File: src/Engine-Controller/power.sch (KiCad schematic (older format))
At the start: 0 parts

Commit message: Completed power supply part of schematic
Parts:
- added C? (x2): 10uF, CWR11C_KEM, symbol Engine-Controller:CWR11HH106KB
- added C?: 22uF, symbol Engine-Controller:UKL1C220KDDANATD
- added C?: 2.2uF, symbol Engine-Controller:CAP_0603
- added C?: 1 uF, symbol Engine-Controller:CAP_0603
- added C?: 10 nF, symbol Engine-Controller:CAP_0603
- added C?: 120uF, symbol Engine-Controller:UHE2A121MHD6
- added D?: LTST-C150GKT, symbol Engine-Controller:LTST-C150GKT
- added D?: Schottky, symbol Engine-Controller:Schottky
- added J?: 4840.2201, CONN_4840.2201_SCH, symbol Engine-Controller:4840.2201
- added L?: 22uH, symbol Engine-Controller:CBC3225T220KR
- added R?: 976, symbol Engine-Controller:RES_0603
- added R?: 240, symbol Engine-Controller:RES_0603
- added R?: 470k, symbol Engine-Controller:RES_0805
- added R?: 1.54k, symbol Engine-Controller:RES_0805
- added U?: LMS8117AMP-3.3_NOPB, symbol Engine-Controller:LMS8117AMP-3.3_NOPB
- added U?: LM22672MRE-5.0_NOPB, symbol Engine-Controller:LM22672MRE-5.0_NOPB
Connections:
- net labels added: 3.3V, 5V, Earth, VIN
- wire segments 0 -> 55

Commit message: Annotated Schematic
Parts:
- gave numbers to parts that had none: 17
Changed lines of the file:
@@
 $EndDescr
 $Comp
-L Engine-Controller:LTST-C150GKT D?
+L Engine-Controller:LTST-C150GKT D3
 U 1 1 60EB9E6E
 P 9300 4350
-F 0 "D?" H 9529 4453 60  0000 L CNN
+F 0 "D3" H 9529 4453 60  0000 L CNN
 F 1 "LTST-C150GKT" H 9529 4347 60  0001 L CNN
 F 2 "" H 9500 3990 60  0001 C CNN
@@
 $EndComp
 $Comp
-L Engine-Controller:CBC3225T220KR L?
+L Engine-Controller:CBC3225T220KR L1
 U 1 1 60EBAB6D
 P 6150 4000
-F 0 "L?" H 6150 4181 50  0000 C CNN
+F 0 "L1" H 6150 4181 50  0000 C CNN
 F 1 "22uH" H 6150 4100 50  0000 C CNN
 F 2 "" H 6000 3800 50  0001 L BNN
@@
 $EndComp
 $Comp
-L Engine-Controller:Schottky D?
+L Engine-Controller:Schottky D2
 U 1 1 60EBB138
 P 5650 4250
-F 0 "D?" V 5650 4330 50  0000 L CNN
+F 0 "D2" V 5650 4330 50  0000 L CNN
 F 1 "Schottky" V 5695 4330 50  0001 L CNN
 F 2 "" H 5650 4250 50  0001 C CNN
@@
 $EndComp
 $Comp
-L Engine-Controller:LMS8117AMP-3.3_NOPB U?
+L Engine-Controller:LMS8117AMP-3.3_NOPB U3
 U 1 1 60EBB9CF
 P 8100 4050
-F 0 "U?" H 8100 4365 50  0000 C CNN
+F 0 "U3" H 8100 4365 50  0000 C CNN
 F 1 "LMS8117AMP-3.3_NOPB" H 8100 4274 50  0000 C CNN
 F 2 "" H 8100 4050 50  0001 C CNN
@@
 $EndComp
 $Comp
-L Engine-Controller:4840.2201 J?
+L Engine-Controller:4840.2201 J1
 U 1 1 60EBBEC5
 P 2450 3500
-F 0 "J?" H 2692 3787 60  0000 C CNN
+F 0 "J1" H 2692 3787 60  0000 C CNN
 F 1 "4840.2201" H 2692 3681 60  0000 C CNN
 F 2 "CONN_4840.2201_SCH" H 2850 2900 60  0001 C CNN
@@
 $EndComp
 $Comp
-L power:Earth #PWR?
+L power:Earth #PWR0103
 U 1 1 60EC7BCD
 P 2600 3950
-F 0 "#PWR?" H 2600 3700 50  0001 C CNN
+F 0 "#PWR0103" H 2600 3700 50  0001 C CNN
 F 1 "Earth" H 2600 3800 50  0001 C CNN
 F 2 "" H 2600 3950 50  0001 C CNN
@@
 	2850 3500 2450 3500
 $Comp
-L Engine-Controller:UKL1C220KDDANATD C?
+L Engine-Controller:UKL1C220KDDANATD C1
 U 1 1 60EDB6C2
 P 2850 3900
-F 0 "C?" H 2965 3946 50  0000 L CNN
+F 0 "C1" H 2965 3946 50  0000 L CNN
 F 1 "22uF" H 2965 3855 50  0000 L CNN
 F 2 "" H 2850 3900 50  0001 C CNN
@@
 	2850 3750 2850 3500
 $Comp
-L power:Earth #PWR?
+L power:Earth #PWR0104
 U 1 1 60EE05FF
 P 2850 4200
-F 0 "#PWR?" H 2850 3950 50  0001 C CNN
+F 0 "#PWR0104" H 2850 3950 50  0001 C CNN
 F 1 "Earth" H 2850 4050 50  0001 C CNN
 F 2 "" H 2850 4200 50  0001 C CNN
@@
 	2850 4050 2850 4200
 $Comp
-L Engine-Controller:CAP_0603 C?
+L Engine-Controller:CAP_0603 C2
 U 1 1 60EE1F59
 P 3300 3900
-F 0 "C?" V 3254 4003 50  0000 L CNN
+F 0 "C2" V 3254 4003 50  0000 L CNN
 F 1 "2.2uF" V 3345 4003 50  0000 L CNN
 F 2 "" H 3200 3500 50  0001 L BNN
@@
 $EndComp
 $Comp
-L power:Earth #PWR?
+L power:Earth #PWR0105
 U 1 1 60EE39C4
 P 3300 4200
-F 0 "#PWR?" H 3300 3950 50  0001 C CNN
+F 0 "#PWR0105" H 3300 3950 50  0001 C CNN
 F 1 "Earth" H 3300 4050 50  0001 C CNN
 F 2 "" H 3300 4200 50  0001 C CNN
@@
 	3300 3750 3300 3500
 $Comp
-L Engine-Controller:RES_0805 R?
+L Engine-Controller:RES_0805 R2
 U 1 1 60EEF47A
 P 3900 3600
-F 0 "R?" H 4050 3700 50  0000 C CNN
+F 0 "R2" H 4050 3700 50  0000 C CNN
 F 1 "470k" H 3800 3700 50  0000 C CNN
 F 2 "" H 3950 3100 50  0001 L BNN
@@
 $EndComp
 $Comp
-L Engine-Controller:CAP_0603 C?
+L Engine-Controller:CAP_0603 C3
 U 1 1 60EF8CF7
 P 4900 4050
-F 0 "C?" V 4854 4153 50  0000 L CNN
+F 0 "C3" V 4854 4153 50  0000 L CNN
 F 1 "1 uF" V 4945 4153 50  0000 L CNN
 F 2 "" H 4800 3650 50  0001 L BNN
@@
 	4900 3800 4900 3900
 $Comp
-L power:Earth #PWR?
+L power:Earth #PWR0106
 U 1 1 60F2A939
 P 4900 4650
-F 0 "#PWR?" H 4900 4400 50  0001 C CNN
+F 0 "#PWR0106" H 4900 4400 50  0001 C CNN
 F 1 "Earth" H 4900 4500 50  0001 C CNN
 F 2 "" H 4900 4650 50  0001 C CNN
@@
 	4900 3700 5400 3700
 $Comp
-L Engine-Controller:CAP_0603 C?
+L Engine-Controller:CAP_0603 C4
 U 1 1 60F34E40
 P 5650 3750
-F 0 "C?" V 5604 3853 50  0000 L CNN
+F 0 "C4" V 5604 3853 50  0000 L CNN
 F 1 "10 nF" V 5695 3853 50  0000 L CNN
 F 2 "" H 5550 3350 50  0001 L BNN
@@
 	4300 3800 4300 3950
 $Comp
-L power:Earth #PWR?
+L power:Earth #PWR0107
 U 1 1 60F261A1
 P 4300 3950
-F 0 "#PWR?" H 4300 3700 50  0001 C CNN
+F 0 "#PWR0107" H 4300 3700 50  0001 C CNN
 F 1 "Earth" H 4300 3800 50  0001 C CNN
 F 2 "" H 4300 3950 50  0001 C CNN
@@
 $EndComp
 $Comp
-L Engine-Controller:LM22672MRE-5.0_NOPB U?
+L Engine-Controller:LM22672MRE-5.0_NOPB U2
 U 1 1 60F0F687
 P 4600 3700
-F 0 "U?" H 4600 4115 50  0000 C CNN
+F 0 "U2" H 4600 4115 50  0000 C CNN
 F 1 "LM22672MRE-5.0_NOPB" H 4600 4024 50  0000 C CNN
 F 2 "" H 4550 3700 50  0001 C CNN
@@
 Connection ~ 5650 4000
 $Comp
-L Engine-Controller:UHE2A121MHD6 C?
+L Engine-Controller:UHE2A121MHD6 C5
 U 1 1 60F87FD5
 P 6650 4250
-F 0 "C?" H 6765 4296 50  0000 L CNN
+F 0 "C5" H 6765 4296 50  0000 L CNN
 F 1 "120uF" H 6765 4205 50  0000 L CNN
 F 2 "" H 6650 4250 50  0001 C CNN
@@
 	6650 4400 6650 4550
 $Comp
-L Engine-Controller:RES_0805 R?
+L Engine-Controller:RES_0805 R4
 U 1 1 60F97080
 P 6650 3700
-F 0 "R?" V 6604 3769 50  0000 L CNN
+F 0 "R4" V 6604 3769 50  0000 L CNN
 F 1 "1.54k" V 6695 3769 50  0000 L CNN
 F 2 "" H 6700 3200 50  0001 L BNN
@@
 	4100 3600 4300 3600
 $Comp
-L Engine-Controller:RES_0603 R?
+L Engine-Controller:RES_0603 R3
 U 1 1 60E5E8D9
 P 5300 4150
-F 0 "R?" V 5254 4219 50  0000 L CNN
+F 0 "R3" V 5254 4219 50  0000 L CNN
 F 1 "976" V 5345 4219 50  0000 L CNN
 F 2 "" H 5350 3650 50  0001 L BNN
@@
 	7300 4000 6650 4000
 $Comp
-L power:Earth #PWR?
+L power:Earth #PWR0108
 U 1 1 60E947DB
 P 8100 4600
-F 0 "#PWR?" H 8100 4350 50  0001 C CNN
+F 0 "#PWR0108" H 8100 4350 50  0001 C CNN
 F 1 "Earth" H 8100 4450 50  0001 C CNN
 F 2 "" H 8100 4600 50  0001 C CNN
@@
 $EndComp
 $Comp
-L Engine-Controller:CWR11HH106KB C?
+L Engine-Controller:CWR11HH106KB C6
 U 1 1 60E95869
 P 7550 4100
-F 0 "C?" V 7647 4205 60  0000 L CNN
+F 0 "C6" V 7647 4205 60  0000 L CNN
 F 1 "10uF" V 7753 4205 60  0000 L CNN
 F 2 "CWR11C_KEM" H 7700 3740 60  0001 C CNN
@@
 	8100 4550 8100 4600
 $Comp
-L Engine-Controller:CWR11HH106KB C?
+L Engine-Controller:CWR11HH106KB C7
 U 1 1 60E9E341
 P 8700 4100
-F 0 "C?" V 8797 4205 60  0000 L CNN
+F 0 "C7" V 8797 4205 60  0000 L CNN
 F 1 "10uF" V 8903 4205 60  0000 L CNN
 F 2 "CWR11C_KEM" H 8850 3740 60  0001 C CNN
@@
 	9300 4000 9800 4000
 $Comp
-L Engine-Controller:RES_0603 R?
+L Engine-Controller:RES_0603 R5
 U 1 1 60ED1BD1
 P 9300 4800
-F 0 "R?" V 9254 4869 50  0000 L CNN
+F 0 "R5" V 9254 4869 50  0000 L CNN
 F 1 "240" V 9345 4869 50  0000 L CNN
 F 2 "" H 9350 4300 50  0001 L BNN
@@
 	9300 4500 9300 4600
 $Comp
-L power:Earth #PWR?
+L power:Earth #PWR0109
 U 1 1 60ED92F3
 P 9300 5100
-F 0 "#PWR?" H 9300 4850 50  0001 C CNN
+F 0 "#PWR0109" H 9300 4850 50  0001 C CNN
 F 1 "Earth" H 9300 4950 50  0001 C CNN
 F 2 "" H 9300 5100 50  0001 C CNN

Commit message: Associated Schematic Symbols with footprints
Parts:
- C1: footprint (none) -> Engine-Controller:UKL1C220KDDANATD
- C2, C3, C4: footprint (none) -> Engine-Controller:CAP_0603
- C5: footprint (none) -> Engine-Controller:UHE2A121MHD6
- C6, C7: footprint CWR11C_KEM -> Engine-Controller:CWR11HH106KB
- D2: footprint (none) -> Engine-Controller:RB160VAM-60TR
- D3: footprint (none) -> Engine-Controller:LTST-C150GKT
- J1: footprint CONN_4840.2201_SCH -> Engine-Controller:12V_power_jack
- L1: footprint (none) -> Engine-Controller:CBC3225T220KR
- R2, R4: footprint (none) -> Engine-Controller:RES_0805
- R3, R5: footprint (none) -> Engine-Controller:RES_0603
- U2: footprint (none) -> Engine-Controller:LM22672MRE-5.0_NOPB
- U3: footprint (none) -> Engine-Controller:SOT-223
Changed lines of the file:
@@
 F 0 "D3" H 9529 4453 60  0000 L CNN
 F 1 "LTST-C150GKT" H 9529 4347 60  0001 L CNN
-F 2 "" H 9500 3990 60  0001 C CNN
+F 2 "Engine-Controller:LTST-C150GKT" H 9500 3990 60  0001 C CNN
 F 3 "" V 9300 4600 60  0000 C CNN
 	1    9300 4350
@@
 F 0 "L1" H 6150 4181 50  0000 C CNN
 F 1 "22uH" H 6150 4100 50  0000 C CNN
-F 2 "" H 6000 3800 50  0001 L BNN
+F 2 "Engine-Controller:CBC3225T220KR" H 6000 3800 50  0001 L BNN
 F 3 "" H 6150 4000 50  0001 L BNN
 	1    6150 4000
@@
 F 0 "D2" V 5650 4330 50  0000 L CNN
 F 1 "Schottky" V 5695 4330 50  0001 L CNN
-F 2 "" H 5650 4250 50  0001 C CNN
+F 2 "Engine-Controller:RB160VAM-60TR" H 5650 4250 50  0001 C CNN
 F 3 "" H 5650 4250 50  0001 C CNN
 	1    5650 4250
@@
 F 0 "U3" H 8100 4365 50  0000 C CNN
 F 1 "LMS8117AMP-3.3_NOPB" H 8100 4274 50  0000 C CNN
-F 2 "" H 8100 4050 50  0001 C CNN
+F 2 "Engine-Controller:SOT-223" H 8100 4050 50  0001 C CNN
 F 3 "" H 8100 4050 50  0001 C CNN
 	1    8100 4050
@@
 F 0 "J1" H 2692 3787 60  0000 C CNN
 F 1 "4840.2201" H 2692 3681 60  0000 C CNN
-F 2 "CONN_4840.2201_SCH" H 2850 2900 60  0001 C CNN
+F 2 "Engine-Controller:12V_power_jack" H 2850 2900 60  0001 C CNN
 F 3 "" H 2450 3500 60  0000 C CNN
 	1    2450 3500
@@
 F 0 "C1" H 2965 3946 50  0000 L CNN
 F 1 "22uF" H 2965 3855 50  0000 L CNN
-F 2 "" H 2850 3900 50  0001 C CNN
+F 2 "Engine-Controller:UKL1C220KDDANATD" H 2850 3900 50  0001 C CNN
 F 3 "~" H 2850 3900 50  0001 C CNN
 	1    2850 3900
@@
 F 0 "C2" V 3254 4003 50  0000 L CNN
 F 1 "2.2uF" V 3345 4003 50  0000 L CNN
-F 2 "" H 3200 3500 50  0001 L BNN
+F 2 "Engine-Controller:CAP_0603" H 3200 3500 50  0001 L BNN
 F 3 "" H 3250 3900 50  0001 L BNN
 	1    3300 3900
@@
 F 0 "R2" H 4050 3700 50  0000 C CNN
 F 1 "470k" H 3800 3700 50  0000 C CNN
-F 2 "" H 3950 3100 50  0001 L BNN
+F 2 "Engine-Controller:RES_0805" H 3950 3100 50  0001 L BNN
 F 3 "" H 3900 3600 50  0001 L BNN
 	1    3900 3600
@@
 F 0 "C3" V 4854 4153 50  0000 L CNN
 F 1 "1 uF" V 4945 4153 50  0000 L CNN
-F 2 "" H 4800 3650 50  0001 L BNN
+F 2 "Engine-Controller:CAP_0603" H 4800 3650 50  0001 L BNN
 F 3 "" H 4850 4050 50  0001 L BNN
 	1    4900 4050
@@
 F 0 "C4" V 5604 3853 50  0000 L CNN
 F 1 "10 nF" V 5695 3853 50  0000 L CNN
-F 2 "" H 5550 3350 50  0001 L BNN
+F 2 "Engine-Controller:CAP_0603" H 5550 3350 50  0001 L BNN
 F 3 "" H 5600 3750 50  0001 L BNN
 	1    5650 3750
@@
 F 0 "U2" H 4600 4115 50  0000 C CNN
 F 1 "LM22672MRE-5.0_NOPB" H 4600 4024 50  0000 C CNN
-F 2 "" H 4550 3700 50  0001 C CNN
+F 2 "Engine-Controller:LM22672MRE-5.0_NOPB" H 4550 3700 50  0001 C CNN
 F 3 "" H 4550 3700 50  0001 C CNN
 	1    4600 3700
@@
 F 0 "C5" H 6765 4296 50  0000 L CNN
 F 1 "120uF" H 6765 4205 50  0000 L CNN
-F 2 "" H 6650 4250 50  0001 C CNN
+F 2 "Engine-Controller:UHE2A121MHD6" H 6650 4250 50  0001 C CNN
 F 3 "~" H 6650 4250 50  0001 C CNN
 	1    6650 4250
@@
 F 0 "R4" V 6604 3769 50  0000 L CNN
 F 1 "1.54k" V 6695 3769 50  0000 L CNN
-F 2 "" H 6700 3200 50  0001 L BNN
+F 2 "Engine-Controller:RES_0805" H 6700 3200 50  0001 L BNN
 F 3 "" H 6650 3700 50  0001 L BNN
 	1    6650 3700
@@
 F 0 "R3" V 5254 4219 50  0000 L CNN
 F 1 "976" V 5345 4219 50  0000 L CNN
-F 2 "" H 5350 3650 50  0001 L BNN
+F 2 "Engine-Controller:RES_0603" H 5350 3650 50  0001 L BNN
 F 3 "" H 5300 4150 50  0001 L BNN
 	1    5300 4150
@@
 F 0 "C6" V 7647 4205 60  0000 L CNN
 F 1 "10uF" V 7753 4205 60  0000 L CNN
-F 2 "CWR11C_KEM" H 7700 3740 60  0001 C CNN
+F 2 "Engine-Controller:CWR11HH106KB" H 7700 3740 60  0001 C CNN
 F 3 "" H 7550 4100 60  0001 C CNN
 	1    7550 4100
@@
 F 0 "C7" V 8797 4205 60  0000 L CNN
 F 1 "10uF" V 8903 4205 60  0000 L CNN
-F 2 "CWR11C_KEM" H 8850 3740 60  0001 C CNN
+F 2 "Engine-Controller:CWR11HH106KB" H 8850 3740 60  0001 C CNN
 F 3 "" H 8700 4100 60  0001 C CNN
 	1    8700 4100
@@
 F 0 "R5" V 9254 4869 50  0000 L CNN
 F 1 "240" V 9345 4869 50  0000 L CNN
-F 2 "" H 9350 4300 50  0001 L BNN
+F 2 "Engine-Controller:RES_0603" H 9350 4300 50  0001 L BNN
 F 3 "" H 9300 4800 50  0001 L BNN
 	1    9300 4800

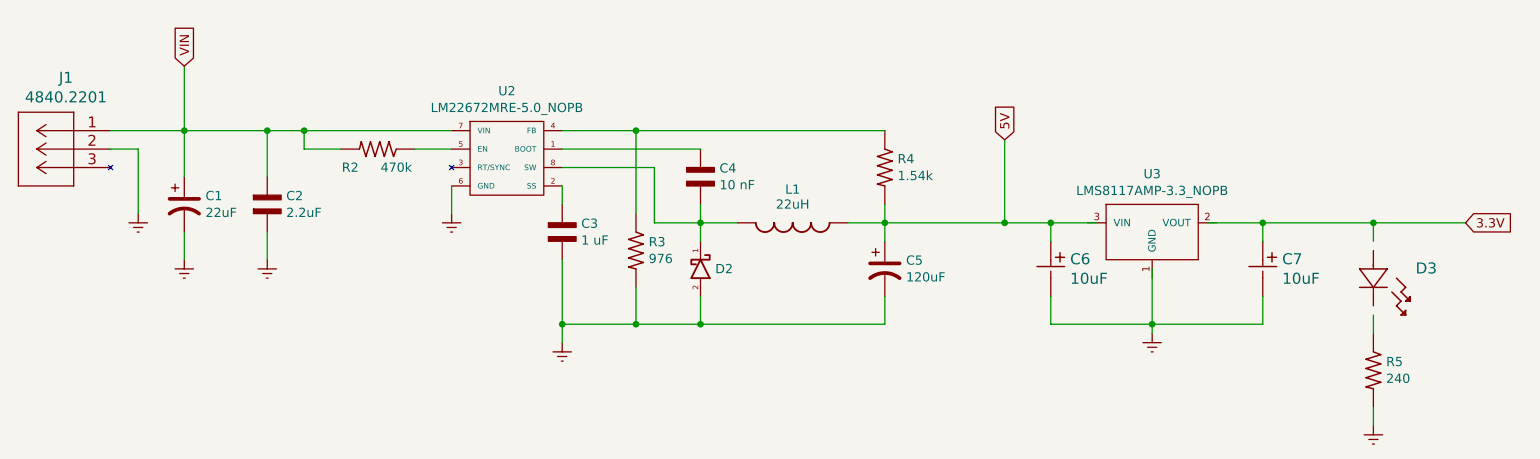
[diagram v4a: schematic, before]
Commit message: Added test points
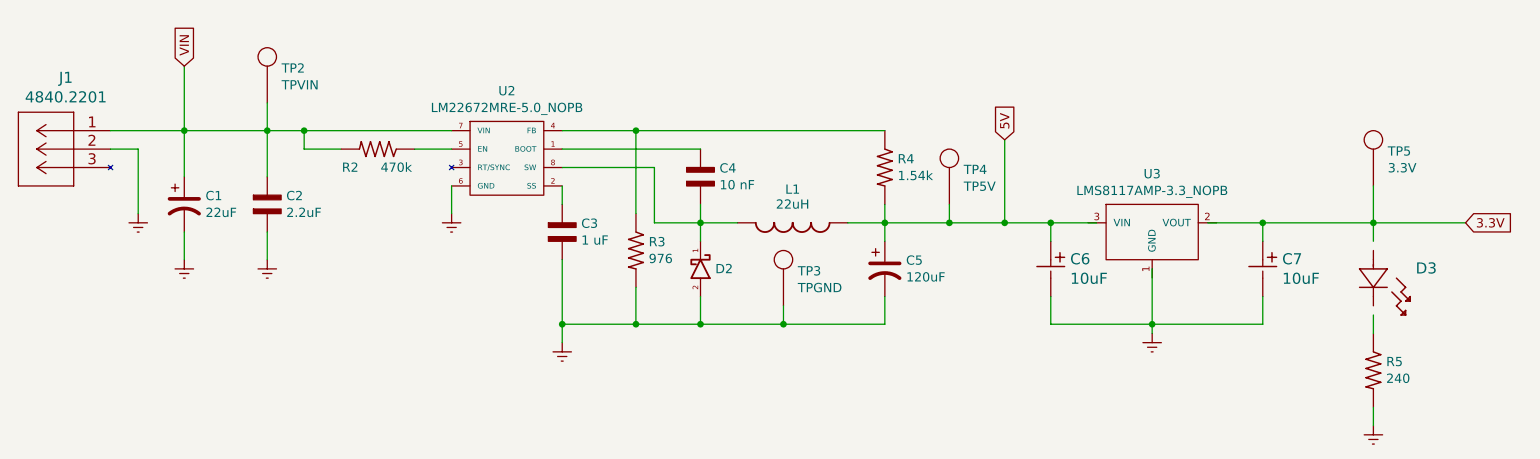
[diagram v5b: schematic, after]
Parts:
- added TP2: TPVIN, symbol Engine-Controller:TP
- added TP3: TPGND, symbol Engine-Controller:TP
- added TP4: TP5V, symbol Engine-Controller:TP
- added TP5: 3.3V, symbol Engine-Controller:TP
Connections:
- wire segments 55 -> 61
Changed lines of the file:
@@
 Connection ~ 5650 4550
 Wire Wire Line
-	5650 4550 6650 4550
+	5650 4550 6100 4550
 Wire Wire Line
 	5300 3950 5300 3500
@@
 Connection ~ 7300 4000
 Wire Wire Line
-	7300 4000 6650 4000
+	7300 4000 7000 4000
 $Comp
 L power:Earth #PWR0108
@@
 	-1   0    0    -1
 $EndComp
+$Comp
+L Engine-Controller:TP TP2
+U 1 1 60E67C30
+P 3300 3350
+F 0 "TP2" H 3378 3538 50  0000 L CNN
+F 1 "TPVIN" H 3378 3447 50  0000 L CNN
+F 2 "" H 3300 3350 50  0001 C CNN
+F 3 "" H 3300 3350 50  0001 C CNN
+	1    3300 3350
+	1    0    0    -1
+$EndComp
+Wire Wire Line
+	3300 3500 3300 3350
+$Comp
+L Engine-Controller:TP TP4
+U 1 1 60E7A9D7
+P 7000 3900
+F 0 "TP4" H 7078 4088 50  0000 L CNN
+F 1 "TP5V" H 7078 3997 50  0000 L CNN
+F 2 "" H 7000 3900 50  0001 C CNN
+F 3 "" H 7000 3900 50  0001 C CNN
+	1    7000 3900
+	1    0    0    -1
+$EndComp
+Wire Wire Line
+	7000 4000 7000 3900
+Connection ~ 7000 4000
+Wire Wire Line
+	7000 4000 6650 4000
+$Comp
+L Engine-Controller:TP TP3
+U 1 1 60E8595F
+P 6100 4450
+F 0 "TP3" H 6178 4638 50  0000 L CNN
+F 1 "TPGND" H 6178 4547 50  0000 L CNN
+F 2 "" H 6100 4450 50  0001 C CNN
+F 3 "" H 6100 4450 50  0001 C CNN
+	1    6100 4450
+	1    0    0    -1
+$EndComp
+Wire Wire Line
+	6100 4550 6100 4450
+Connection ~ 6100 4550
+Wire Wire Line
+	6100 4550 6650 4550
+$Comp
+L Engine-Controller:TP TP5
+U 1 1 60E93926
+P 9300 3800
+F 0 "TP5" H 9378 3988 50  0000 L CNN
+F 1 "3.3V" H 9378 3897 50  0000 L CNN
+F 2 "" H 9300 3800 50  0001 C CNN
+F 3 "" H 9300 3800 50  0001 C CNN
+	1    9300 3800
+	1    0    0    -1
+$EndComp
+Wire Wire Line
+	9300 3800 9300 4000
 $EndSCHEMATC

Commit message: Imported footprints into layout file
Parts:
- TP2, TP3, TP4, TP5: footprint (none) -> Engine-Controller:TP
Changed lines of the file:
@@
 F 0 "TP2" H 3378 3538 50  0000 L CNN
 F 1 "TPVIN" H 3378 3447 50  0000 L CNN
-F 2 "" H 3300 3350 50  0001 C CNN
+F 2 "Engine-Controller:TP" H 3300 3350 50  0001 C CNN
 F 3 "" H 3300 3350 50  0001 C CNN
 	1    3300 3350
@@
 F 0 "TP4" H 7078 4088 50  0000 L CNN
 F 1 "TP5V" H 7078 3997 50  0000 L CNN
-F 2 "" H 7000 3900 50  0001 C CNN
+F 2 "Engine-Controller:TP" H 7000 3900 50  0001 C CNN
 F 3 "" H 7000 3900 50  0001 C CNN
 	1    7000 3900
@@
 F 0 "TP3" H 6178 4638 50  0000 L CNN
 F 1 "TPGND" H 6178 4547 50  0000 L CNN
-F 2 "" H 6100 4450 50  0001 C CNN
+F 2 "Engine-Controller:TP" H 6100 4450 50  0001 C CNN
 F 3 "" H 6100 4450 50  0001 C CNN
 	1    6100 4450
@@
 F 0 "TP5" H 9378 3988 50  0000 L CNN
 F 1 "3.3V" H 9378 3897 50  0000 L CNN
-F 2 "" H 9300 3800 50  0001 C CNN
+F 2 "Engine-Controller:TP" H 9300 3800 50  0001 C CNN
 F 3 "" H 9300 3800 50  0001 C CNN
 	1    9300 3800
